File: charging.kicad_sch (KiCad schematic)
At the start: 14 parts, among them J5 S2B-PH-SM4-TB, U2 BQ24075RGT

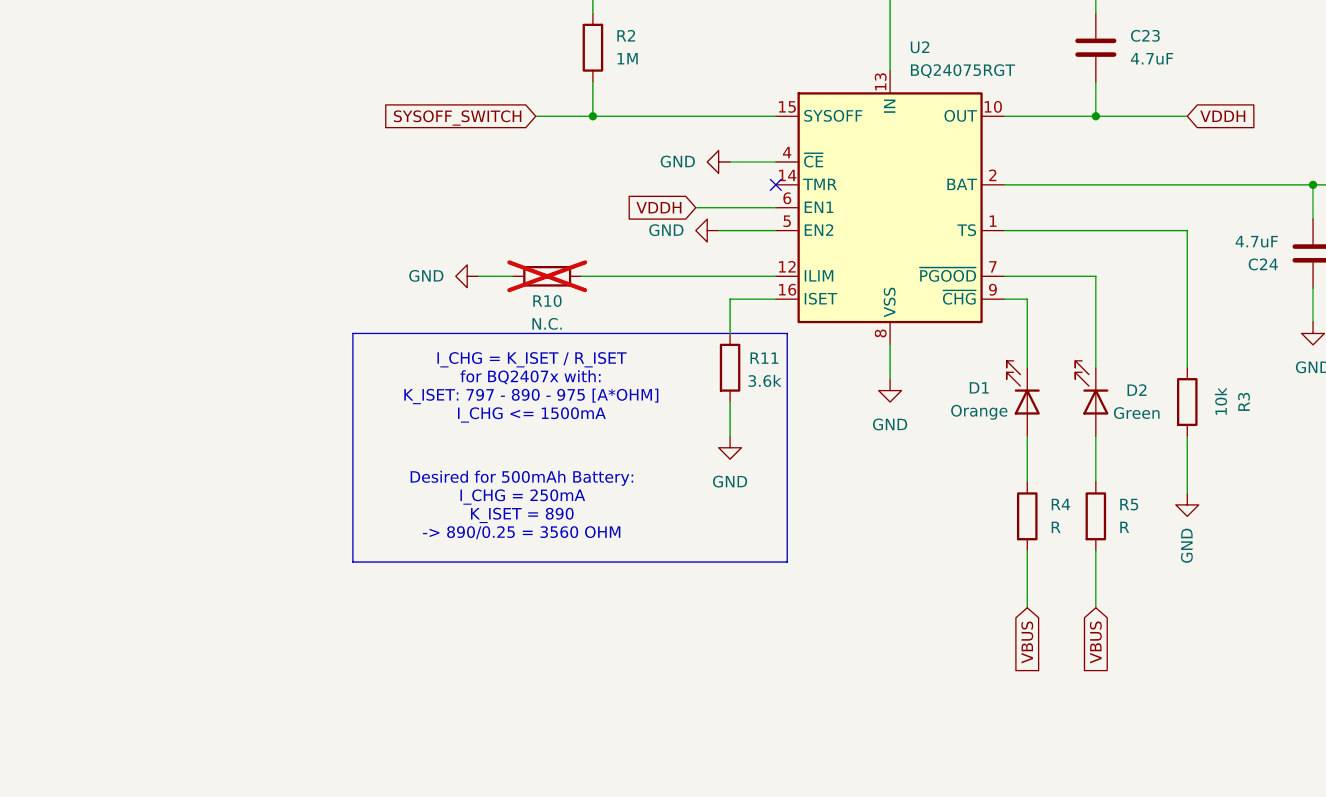
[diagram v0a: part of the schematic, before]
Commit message: Adjusted Footprint sizes
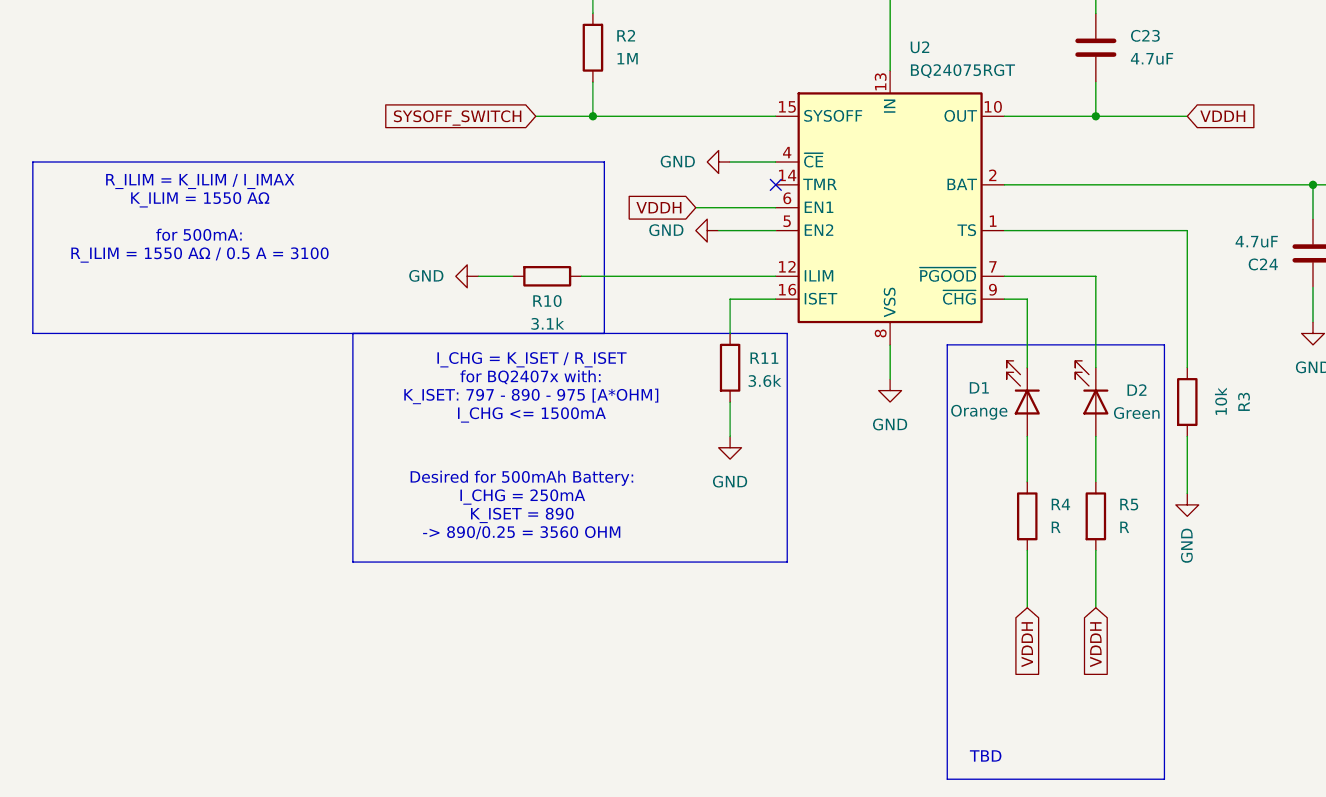
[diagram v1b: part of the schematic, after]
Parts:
- C23: footprint Capacitor_SMD:C_0402_1005Metric -> Capacitor_SMD:C_0603_1608Metric
- R10: value N.C. -> 3.1k; footprint Resistor_SMD:R_0603_1608Metric -> Resistor_SMD:R_0402_1005Metric; now fitted
- R11, R2, R3, R4, R5: footprint Resistor_SMD:R_0603_1608Metric -> Resistor_SMD:R_0402_1005Metric
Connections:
- net VBUS: no longer R4.2, R5.2
- net VDDH: now also R4.2, R5.2
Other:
- note added: "R_ILIM = K_ILIM / I_IMAX K_ILIM = 1550 AΩ for 500mA: R_ILIM = 1550 AΩ / 0.5 A = 3100"
- note added: "TBD"
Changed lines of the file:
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@@
 	(paper "A4")
+	(rectangle
+		(start 46.99 82.55)
+		(end 110.49 101.6)
+		(stroke
+			(width 0)
+			(type default)
+		)
+		(fill
+			(type none)
+		)
+	)
 	(rectangle
 		(start 82.55 101.6)
 		(end 130.81 127)
+		(stroke
+			(width 0)
+			(type default)
+		)
+		(fill
+			(type none)
+		)
+	)
+	(rectangle
+		(start 148.59 102.87)
+		(end 172.72 151.13)
 		(stroke
 			(width 0)
@@
 		(exclude_from_sim no)
 		(at 102.362 107.696 0)
+		(effects
+			(font
+				(size 1.27 1.27)
+			)
+		)
+	)
+	(text "TBD"
+		(exclude_from_sim no)
+		(at 152.908 148.844 0)
+		(effects
+			(font
+				(size 1.27 1.27)
+			)
+		)
+	)
+	(text "R_ILIM = K_ILIM / I_IMAX\nK_ILIM = 1550 AΩ\n\nfor 500mA:\nR_ILIM = 1550 AΩ / 0.5 A = 3100"
+		(exclude_from_sim no)
+		(at 65.532 88.9 0)
 		(effects
 			(font
@@
 		)
 	)
-	(global_label "VBUS"
+	(global_label "VDDH"
 		(shape input)
-		(at 157.48 132.08 270)
+		(at 175.26 77.47 0)
 		(fields_autoplaced yes)
 		(effects
@@
 				(size 1.27 1.27)
 			)
-			(justify right)
+			(justify left)
 		)
 		(property "Intersheetrefs" "${INTERSHEET_REFS}"
-			(at 157.48 139.9638 90)
-			(effects
-				(font
-					(size 1.27 1.27)
-				)
-				(justify right)
-				(hide yes)
-			)
-		)
-	)
-	(global_label "VDDH"
+			(at 183.2043 77.47 0)
+			(effects
+				(font
+					(size 1.27 1.27)
+				)
+				(justify left)
+				(hide yes)
+			)
+		)
+	)
+	(global_label "VBAT"
 		(shape input)
-		(at 175.26 77.47 0)
+		(at 194.31 85.09 0)
 		(fields_autoplaced yes)
 		(effects
@@
 		)
 		(property "Intersheetrefs" "${INTERSHEET_REFS}"
-			(at 183.2043 77.47 0)
+			(at 201.71 85.09 0)
 			(effects
 				(font
@@
 		)
 	)
-	(global_label "VBAT"
+	(global_label "VBUS"
 		(shape input)
-		(at 194.31 85.09 0)
+		(at 142.24 58.42 90)
 		(fields_autoplaced yes)
 		(effects
@@
 		)
 		(property "Intersheetrefs" "${INTERSHEET_REFS}"
-			(at 201.71 85.09 0)
+			(at 142.24 50.5362 90)
 			(effects
 				(font
@@
 		)
 	)
-	(global_label "VBUS"
+	(global_label "VDDH"
 		(shape input)
-		(at 142.24 58.42 90)
+		(at 165.1 132.08 270)
 		(fields_autoplaced yes)
 		(effects
@@
 				(size 1.27 1.27)
 			)
-			(justify left)
+			(justify right)
 		)
 		(property "Intersheetrefs" "${INTERSHEET_REFS}"
-			(at 142.24 50.5362 90)
-			(effects
-				(font
-					(size 1.27 1.27)
-				)
-				(justify left)
-				(hide yes)
-			)
-		)
-	)
-	(global_label "VBUS"
+			(at 165.1 140.0243 90)
+			(effects
+				(font
+					(size 1.27 1.27)
+				)
+				(justify right)
+				(hide yes)
+			)
+		)
+	)
+	(global_label "VDDH"
 		(shape input)
-		(at 165.1 132.08 270)
+		(at 157.48 132.08 270)
 		(fields_autoplaced yes)
 		(effects
@@
 		)
 		(property "Intersheetrefs" "${INTERSHEET_REFS}"
-			(at 165.1 139.9638 90)
+			(at 157.48 140.0243 90)
 			(effects
 				(font
@@
 			)
 		)
-		(property "Footprint" "Resistor_SMD:R_0603_1608Metric"
+		(property "Footprint" "Resistor_SMD:R_0402_1005Metric"
 			(at 122.682 105.41 90)
 			(effects
@@
 			)
 		)
-		(property "Footprint" "Capacitor_SMD:C_0402_1005Metric"
+		(property "Footprint" "Capacitor_SMD:C_0603_1608Metric"
 			(at 164.1348 66.04 0)
 			(effects
@@
 			)
 		)
-		(property "Footprint" "Resistor_SMD:R_0603_1608Metric"
+		(property "Footprint" "Resistor_SMD:R_0402_1005Metric"
 			(at 173.482 109.22 90)
 			(effects
@@
 			)
 		)
-		(property "Footprint" "Resistor_SMD:R_0603_1608Metric"
+		(property "Footprint" "Resistor_SMD:R_0402_1005Metric"
 			(at 110.998 69.85 90)
 			(effects
@@
 		(in_bom yes)
 		(on_board yes)
-		(dnp yes)
+		(dnp no)
 		(property "Reference" "R10"
 			(at 104.14 98.044 90)
@@
 			)
 		)
-		(property "Value" "N.C."
+		(property "Value" "3.1k"
 			(at 104.14 100.584 90)
 			(effects
@@
 			)
 		)
-		(property "Footprint" "Resistor_SMD:R_0603_1608Metric"
+		(property "Footprint" "Resistor_SMD:R_0402_1005Metric"
 			(at 104.14 93.472 90)
 			(effects
@@
 			)
 		)
-		(property "Footprint" "Resistor_SMD:R_0603_1608Metric"
+		(property "Footprint" "Resistor_SMD:R_0402_1005Metric"
 			(at 163.322 121.92 90)
 			(effects
@@
 			)
 		)
-		(property "Footprint" "Resistor_SMD:R_0603_1608Metric"
+		(property "Footprint" "Resistor_SMD:R_0402_1005Metric"
 			(at 155.702 121.92 90)
 			(effects

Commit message: Started PCB design
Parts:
- D1: value Orange -> LTST-C170KFKT
- D2: value Green -> LTST-C170KGKT
- R4, R5: value R -> 1k
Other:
- note added: "R=(V-V_F_LED)/I V=5.5 LTST-C170KFKT: I=10mA, V=2.0 R=3.5/0.01=350 LTST-C170KGKT: I=10mA, V=2.0 R=3.5/0.01=350"
- note removed: "TBD"
- moved on the sheet: C24, D1, D2, R3, R4, R5

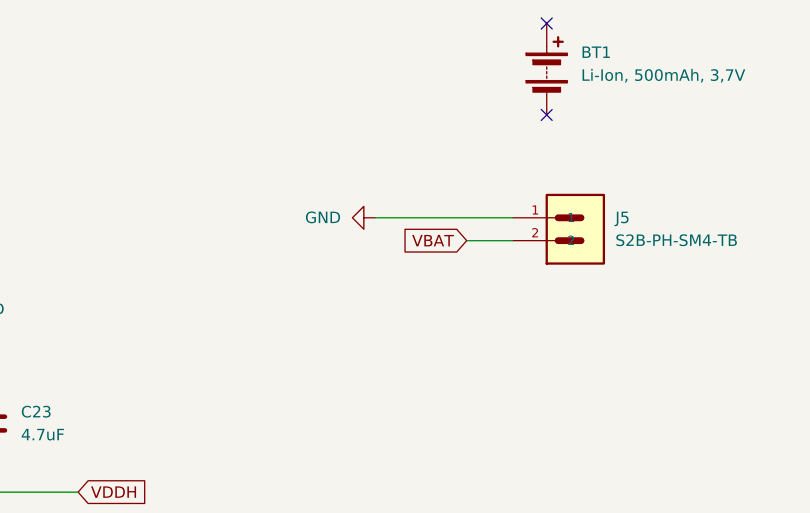
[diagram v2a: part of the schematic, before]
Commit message: DFM problems to solve; CE compliance issue
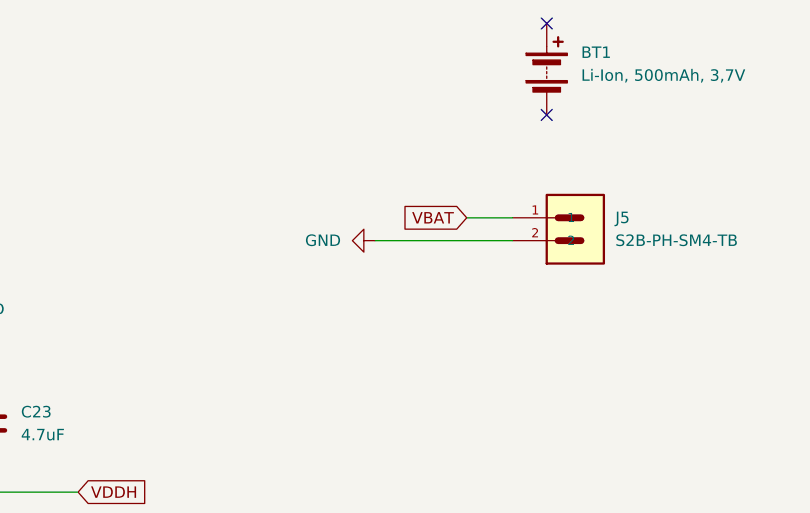
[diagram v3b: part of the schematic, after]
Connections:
- net GND: now also J5.2; no longer J5.1
- net VBAT: now also J5.1; no longer J5.2
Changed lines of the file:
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@@
 	(wire
 		(pts
-			(xy 208.28 46.99) (xy 223.52 46.99)
+			(xy 208.28 49.53) (xy 223.52 49.53)
 		)
 		(stroke
@@
 	(wire
 		(pts
-			(xy 234.95 85.09) (xy 240.03 85.09)
+			(xy 218.44 46.99) (xy 223.52 46.99)
 		)
 		(stroke
@@
 	(wire
 		(pts
-			(xy 156.21 113.03) (xy 156.21 118.11)
+			(xy 234.95 85.09) (xy 240.03 85.09)
 		)
 		(stroke
@@
 	(wire
 		(pts
-			(xy 124.46 109.22) (xy 124.46 113.03)
+			(xy 156.21 113.03) (xy 156.21 118.11)
 		)
 		(stroke
@@
 	(wire
 		(pts
-			(xy 142.24 58.42) (xy 142.24 60.96)
+			(xy 124.46 109.22) (xy 124.46 113.03)
 		)
 		(stroke
@@
 	(wire
 		(pts
-			(xy 138.43 60.96) (xy 142.24 60.96)
+			(xy 142.24 58.42) (xy 142.24 60.96)
 		)
 		(stroke
@@
 	(wire
 		(pts
-			(xy 193.04 113.03) (xy 193.04 118.11)
+			(xy 138.43 60.96) (xy 142.24 60.96)
 		)
 		(stroke
@@
 	(wire
 		(pts
-			(xy 156.21 97.79) (xy 156.21 105.41)
+			(xy 193.04 113.03) (xy 193.04 118.11)
 		)
 		(stroke
@@
 	(wire
 		(pts
-			(xy 109.22 62.23) (xy 109.22 66.04)
+			(xy 156.21 97.79) (xy 156.21 105.41)
 		)
 		(stroke
@@
 	(wire
 		(pts
-			(xy 154.94 85.09) (xy 234.95 85.09)
+			(xy 109.22 62.23) (xy 109.22 66.04)
 		)
 		(stroke
@@
 	(wire
 		(pts
-			(xy 218.44 49.53) (xy 223.52 49.53)
+			(xy 154.94 85.09) (xy 234.95 85.09)
 		)
 		(stroke
@@
 	(global_label "VBAT"
 		(shape input)
-		(at 218.44 49.53 180)
+		(at 218.44 46.99 180)
 		(fields_autoplaced yes)
 		(effects
@@
 		)
 		(property "Intersheetrefs" "${INTERSHEET_REFS}"
-			(at 211.04 49.53 0)
+			(at 211.04 46.99 0)
 			(effects
 				(font
@@
 	(symbol
 		(lib_id "power:GND")
-		(at 208.28 46.99 270)
+		(at 208.28 49.53 270)
 		(unit 1)
 		(exclude_from_sim no)
@@
 		(fields_autoplaced yes)
 		(property "Reference" "#PWR036"
-			(at 201.93 46.99 0)
+			(at 201.93 49.53 0)
 			(effects
 				(font
@@
 		)
 		(property "Value" "GND"
-			(at 204.47 46.9899 90)
+			(at 204.47 49.5299 90)
 			(effects
 				(font
@@
 		)
 		(property "Footprint" ""
-			(at 208.28 46.99 0)
+			(at 208.28 49.53 0)
 			(effects
 				(font
@@
 		)
 		(property "Datasheet" ""
-			(at 208.28 46.99 0)
+			(at 208.28 49.53 0)
 			(effects
 				(font
@@
 		)
 		(property "Description" "Power symbol creates a global label with name \"GND\" , ground"
-			(at 208.28 46.99 0)
-			(effects
-				(font
+			(at 208.28 49.53 0)
+			(effects
+				(font
